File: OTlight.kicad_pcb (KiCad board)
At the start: 2 copper layers, 90 x 55 mm, 70 parts, among them P1 CONN_01X02, P2 CONN_01X14, P3 CONN_01X14, P4 CONN_01X14, P5 CONN_01X14, Q1 TEMT6000, Q2 RSR030N06TL, T1 TRANSFO, U1 LM3478, U12 MAX6931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

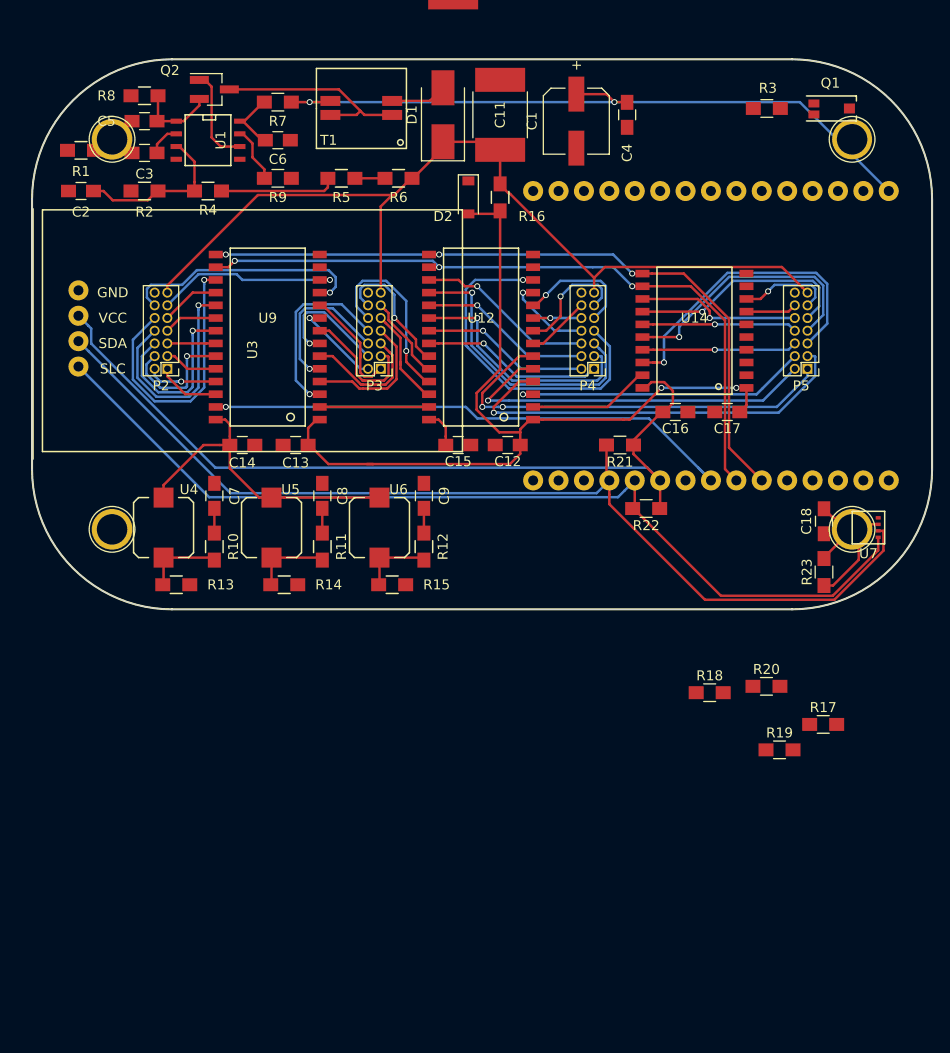
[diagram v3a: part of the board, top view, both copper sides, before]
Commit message: The start of bearing upgrade
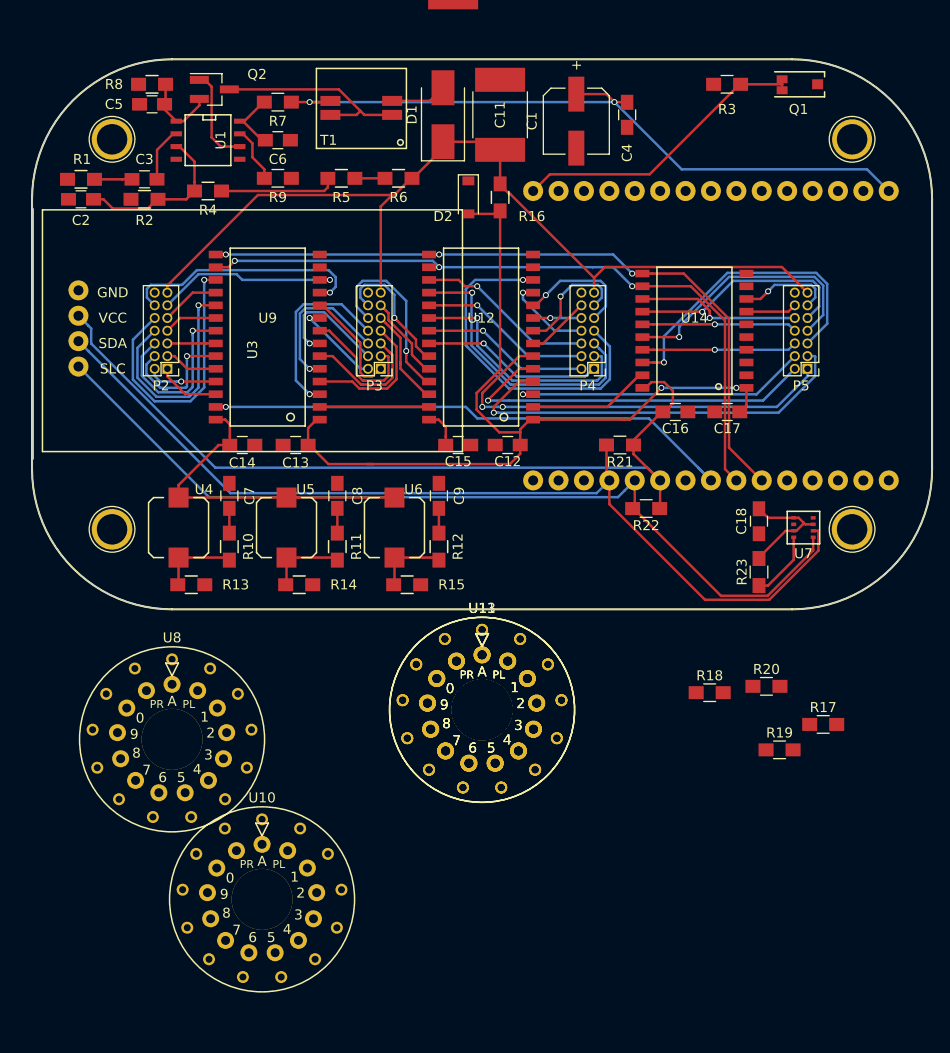
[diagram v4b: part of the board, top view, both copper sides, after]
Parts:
- added U10: IN-14, BamboulabFootprints:IN-14-bearing-7mm, F.Cu at (67.0, 161.0)
- added U11, U13: IN-14, BamboulabFootprints:IN-14-bearing-7mm, F.Cu at (89.0, 142.1)
- added U8: IN-14, BamboulabFootprints:IN-14-bearing-7mm, F.Cu at (58.0, 145.0)
- moved C18 6.50 mm to (116.7, 123.2)
- moved R23 6.50 mm to (116.7, 128.3)
- moved U7 6.50 mm to (121.1, 123.8)
- moved R3 4.65 mm to (113.5, 79.5)
- moved Q1 3.99 mm to (119.0, 79.5)
- moved R1 2.89 mm to (48.9, 89.0)
- moved C3 2.64 mm to (55.2, 89.0)
- moved C5 1.85 mm to (56.0, 81.5)
- moved C7 1.50 mm to (63.7, 120.7)
- moved C8 1.50 mm to (74.5, 120.7)
- moved C9 1.50 mm to (84.7, 120.7)
- moved R10 1.50 mm to (63.7, 125.7)
- moved R11 1.50 mm to (74.5, 125.7)
- moved R12 1.50 mm to (84.7, 125.7)
- moved R13 1.50 mm to (59.9, 129.5)
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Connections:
- R17 pad 1: Net-(R17-Pad1) -> /HVout
- R18 pad 1: Net-(R18-Pad1) -> /HVout
- R19 pad 1: Net-(R19-Pad1) -> /HVout
- R20 pad 1: Net-(R20-Pad1) -> /HVout
- U12 pad 10: Net-(P4-Pad9) -> Net-(U11-Pad10)
- U12 pad 11: Net-(P4-Pad8) -> Net-(U11-Pad9)
- U12 pad 12: Net-(P4-Pad7) -> Net-(U11-Pad8)
- U12 pad 17: Net-(P4-Pad6) -> Net-(U11-Pad7)
- U12 pad 18: Net-(P4-Pad5) -> Net-(U11-Pad6)
- U12 pad 19: Net-(P4-Pad4) -> Net-(U11-Pad5)
- U12 pad 20: Net-(P4-Pad3) -> Net-(U11-Pad4)
- U12 pad 21: Net-(P4-Pad2) -> Net-(U11-Pad3)
- U12 pad 22: Net-(P4-Pad1) -> Net-(U11-Pad12)
- U12 pad 23: Net-(P3-Pad12) -> Net-(U10-Pad13)
- U12 pad 24: Net-(P3-Pad11) -> Net-(U10-Pad2)
- U12 pad 25: Net-(P3-Pad10) -> Net-(U10-Pad11)
- U12 pad 26: Net-(P3-Pad9) -> Net-(U10-Pad10)
- U12 pad 3: Net-(P5-Pad4) -> Net-(U12-Pad3)
- U12 pad 4: Net-(P5-Pad3) -> Net-(U12-Pad4)
- U12 pad 5: Net-(P5-Pad2) -> Net-(U12-Pad5)
- U12 pad 6: Net-(P5-Pad1) -> Net-(U12-Pad6)
- U12 pad 7: Net-(P4-Pad12) -> Net-(U11-Pad13)
- U12 pad 8: Net-(P4-Pad11) -> Net-(U11-Pad2)
- U12 pad 9: Net-(P4-Pad10) -> Net-(U11-Pad11)
- U14 pad 13: Net-(P5-Pad10) -> Net-(U13-Pad11)
- U14 pad 14: Net-(P5-Pad9) -> Net-(U13-Pad10)
- U14 pad 15: Net-(P5-Pad8) -> Net-(U13-Pad9)
- U14 pad 16: Net-(P5-Pad7) -> Net-(U13-Pad8)
- U14 pad 17: Net-(P5-Pad6) -> Net-(U13-Pad7)
- U14 pad 18: Net-(P5-Pad5) -> Net-(U13-Pad6)
- U14 pad 7: Net-(P5-Pad12) -> Net-(U13-Pad13)
- U14 pad 8: Net-(P5-Pad11) -> Net-(U13-Pad2)
- U9 pad 10: Net-(P3-Pad1) -> Net-(U10-Pad12)
- U9 pad 11: Net-(P2-Pad12) -> Net-(U8-Pad13)
- U9 pad 12: Net-(P2-Pad11) -> Net-(U8-Pad2)
- U9 pad 17: Net-(P2-Pad10) -> Net-(U8-Pad11)
- U9 pad 18: Net-(P2-Pad9) -> Net-(U8-Pad10)
- U9 pad 19: Net-(P2-Pad8) -> Net-(U8-Pad9)
- U9 pad 20: Net-(P2-Pad7) -> Net-(U8-Pad8)
- U9 pad 21: Net-(P2-Pad6) -> Net-(U8-Pad7)
- U9 pad 22: Net-(P2-Pad5) -> Net-(U8-Pad6)
- U9 pad 23: Net-(P2-Pad4) -> Net-(U8-Pad5)
- U9 pad 24: Net-(P2-Pad3) -> Net-(U8-Pad4)
- U9 pad 25: Net-(P2-Pad2) -> Net-(U8-Pad3)
- U9 pad 26: Net-(P2-Pad1) -> Net-(U8-Pad12)
- U9 pad 3: Net-(P3-Pad8) -> Net-(U10-Pad9)
- U9 pad 4: Net-(P3-Pad7) -> Net-(U10-Pad8)
- U9 pad 5: Net-(P3-Pad6) -> Net-(U10-Pad7)
- U9 pad 6: Net-(P3-Pad5) -> Net-(U10-Pad6)
- U9 pad 7: Net-(P3-Pad4) -> Net-(U10-Pad5)
- U9 pad 8: Net-(P3-Pad3) -> Net-(U10-Pad4)
- U9 pad 9: Net-(P3-Pad2) -> Net-(U10-Pad3)
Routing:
- net Net-(Q1-Pad2): track 0.00 -> 30.4 mm
- net Net-(R22-Pad2): track 96.0 -> 89.5 mm
- net Net-(R21-Pad2): track 101.8 -> 95.3 mm
- net Net-(U13-Pad10): track 0.00 -> 5.96 mm
- net Net-(P5-Pad9): track 22.8 -> 16.8 mm
- net Net-(U11-Pad8): track 0.00 -> 5.80 mm, vias 0 -> 1
- net Net-(P4-Pad7): track 35.0 -> 29.2 mm, vias 1 -> 0
- net Net-(P3-Pad1): track 11.5 -> 5.91 mm
- net Net-(U10-Pad12): track 0.00 -> 5.61 mm
- net Net-(U13-Pad11): track 0.00 -> 5.54 mm
- net Net-(P5-Pad10): track 16.4 -> 10.9 mm
- net Net-(U11-Pad3): track 0.00 -> 5.39 mm
- net Net-(P4-Pad2): track 16.8 -> 11.4 mm
- net Net-(P4-Pad3): track 24.4 -> 19.6 mm
- net Net-(U11-Pad4): track 0.00 -> 4.82 mm
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
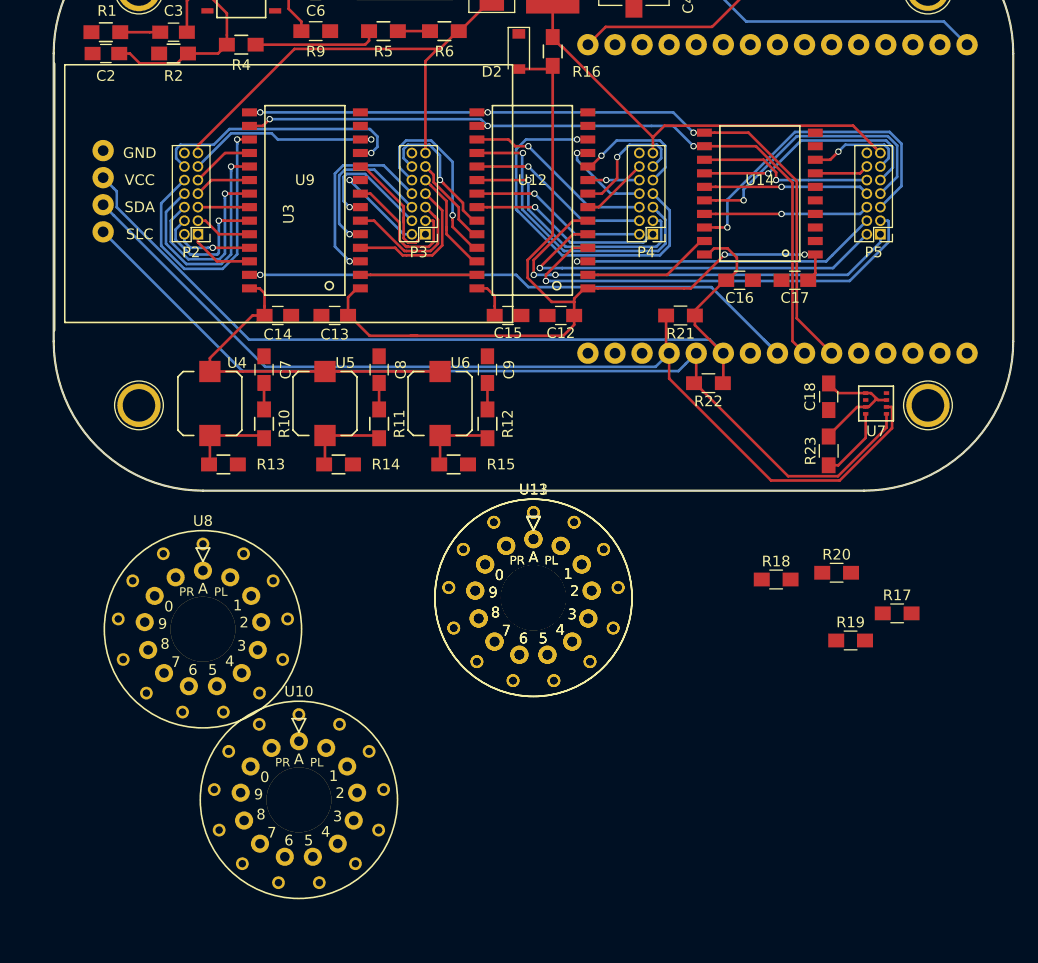
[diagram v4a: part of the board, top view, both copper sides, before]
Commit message: Realigned tubes with bearings, now the tubes are perfectly centered on both x and y axis
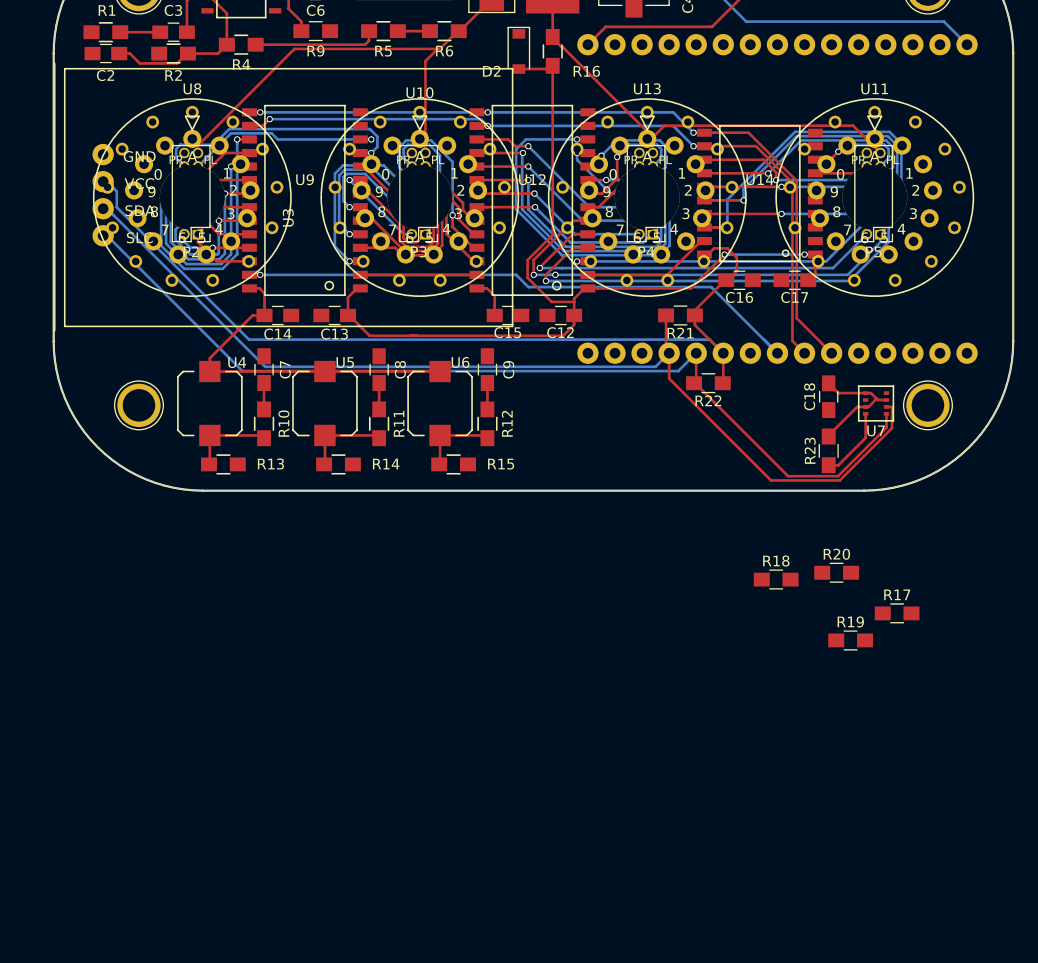
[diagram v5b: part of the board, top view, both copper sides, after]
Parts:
- moved U10 57.6 mm to (78.3, 104.5)
- moved U11 49.3 mm to (121.0, 104.5)
- moved U8 40.5 mm to (57.0, 104.5)
- moved U13 39.0 mm to (99.7, 104.5)
- moved U3 0.37 mm to (66.0, 104.5)
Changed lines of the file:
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@@
-(kicad_pcb (version 4) (host pcbnew 4.0.7)
+(kicad_pcb (version 20171130) (host pcbnew "(2018-01-14 revision 63e55e918)-makepkg")
   (general
-    (links 239)
-    (no_connects 161)
-    (area 43.949999 76.949999 134.050001 132.050001)
     (thickness 1.6)
     (drawings 19)
@@
       (layerselection 0x000f0_80000001)
       (usegerberextensions false)
+      (usegerberattributes false)
+      (usegerberadvancedattributes false)
+      (creategerberjobfile false)
       (excludeedgelayer true)
       (linewidth 0.100000)
@@
       (hpglpenspeed 20)
       (hpglpendiameter 15)
-      (hpglpenoverlay 2)
       (psnegative false)
       (psa4output false)
@@
     (tags "resistor 0805")
     (attr smd)
-    (fp_text reference R12 (at 0 -1.905 450) (layer F.SilkS)
+    (fp_text reference R12 (at 0 -1.905 90) (layer F.SilkS)
       (effects (font (size 1 1) (thickness 0.15)))
     )
@@
     (tags SOD-123)
     (attr smd)
-    (fp_text reference D2 (at 1.905 2.54 540) (layer F.SilkS)
+    (fp_text reference D2 (at 1.905 2.54 180) (layer F.SilkS)
       (effects (font (size 1 1) (thickness 0.15)))
     )
@@
     (tags "capacitor 0805")
     (attr smd)
-    (fp_text reference C4 (at 3.81 0 450) (layer F.SilkS)
+    (fp_text reference C4 (at 3.81 0 90) (layer F.SilkS)
       (effects (font (size 1 1) (thickness 0.15)))
     )
@@
     (tags "resistor 0805")
     (attr smd)
-    (fp_text reference R8 (at 3.81 0 360) (layer F.SilkS)
+    (fp_text reference R8 (at 3.81 0) (layer F.SilkS)
       (effects (font (size 1 1) (thickness 0.15)))
     )
@@
     (tags "resistor 0805")
     (attr smd)
-    (fp_text reference R10 (at 0 -1.905 450) (layer F.SilkS)
+    (fp_text reference R10 (at 0 -1.905 90) (layer F.SilkS)
       (effects (font (size 1 1) (thickness 0.15)))
     )
@@
     (tags "resistor 0805")
     (attr smd)
-    (fp_text reference R16 (at 1.905 -3.175 360) (layer F.SilkS)
+    (fp_text reference R16 (at 1.905 -3.175) (layer F.SilkS)
       (effects (font (size 1 1) (thickness 0.15)))
     )
@@
     (at 26.5176 110.6932)
     (fp_text reference G*** (at 0 0) (layer F.SilkS) hide
-      (effects (font (thickness 0.3)))
+      (effects (font (size 1.524 1.524) (thickness 0.3)))
     )
     (fp_text value LOGO (at 0.75 0) (layer F.SilkS) hide
-      (effects (font (thickness 0.3)))
+      (effects (font (size 1.524 1.524) (thickness 0.3)))
     )
     (fp_poly (pts (xy 0.066496 -3.18191) (xy 0.14042 -3.180865) (xy 0.20835 -3.178867) (xy 0.267395 -3.175902)
@@
       (net 2 GND))
     (model ${KISYS3DMOD}/Pin_Headers.3dshapes/Pin_Header_Straight_1x02_Pitch2.54mm.wrl
-      (at (xyz 0 -0.05 0))
+      (offset (xyz 0 -1.269999980926514 0))
       (scale (xyz 1 1 1))
       (rotate (xyz 0 0 90))
@@
     (at 73.914 192.405)
     (fp_text reference G*** (at 0 0) (layer F.SilkS) hide
-      (effects (font (thickness 0.3)))
+      (effects (font (size 1.524 1.524) (thickness 0.3)))
     )
     (fp_text value LOGO (at 0.75 0) (layer F.SilkS) hide
-      (effects (font (thickness 0.3)))
+      (effects (font (size 1.524 1.524) (thickness 0.3)))
     )
     (fp_poly (pts (xy 7.776308 2.422769) (xy -7.776307 2.422769) (xy -7.776307 1.008304) (xy -7.655194 1.008304)
@@
     (at 144.272 130.048)
     (fp_text reference G*** (at 0 0) (layer F.SilkS) hide
-      (effects (font (thickness 0.3)))
+      (effects (font (size 1.524 1.524) (thickness 0.3)))
     )
     (fp_text value LOGO (at 0.75 0) (layer F.SilkS) hide
-      (effects (font (thickness 0.3)))
+      (effects (font (size 1.524 1.524) (thickness 0.3)))
     )
     (fp_poly (pts (xy -2.603459 -0.236601) (xy -2.492479 -0.183516) (xy -2.407788 -0.092057) (xy -2.355584 0.03253)
@@
     (at 119.253 32.131)
     (fp_text reference G*** (at 0 0) (layer F.SilkS) hide
-      (effects (font (thickness 0.3)))
+      (effects (font (size 1.524 1.524) (thickness 0.3)))
     )
     (fp_text value LOGO (at 0.75 0) (layer F.SilkS) hide
-      (effects (font (thickness 0.3)))
+      (effects (font (size 1.524 1.524) (thickness 0.3)))
     )
     (fp_poly (pts (xy 4.301613 4.301613) (xy -4.301612 4.301613) (xy -4.301612 2.335162) (xy -4.055806 2.335162)
@@
   )
   (module BamboulabFootprints:DS3231 (layer F.Cu)
-    (at 66.04 104.14)
+    (at 66.04 104.51)
     (fp_text reference U3 (at 0 1.905 90) (layer F.SilkS)
       (effects (font (size 1 1) (thickness 0.15)))
@@
   )
   (module BamboulabFootprints:IN-14-bearing-7mm locked (layer F.Cu)
-    (at 58 145)
+    (at 57.004 104.51)
     (fp_text reference U8 (at 0 -10.16) (layer F.SilkS)
       (effects (font (size 1 1) (thickness 0.15)))
@@
   )
   (module BamboulabFootprints:IN-14-bearing-7mm locked (layer F.Cu)
-    (at 67 161)
-    (fp_text reference U10 (at 0 -10.16) (layer F.SilkS)
+    (at 78.34 104.51)
+    (fp_text reference U10 (at 0 -9.79) (layer F.SilkS)
       (effects (font (size 1 1) (thickness 0.15)))
     )
@@
   )
   (module BamboulabFootprints:IN-14-bearing-7mm locked (layer F.Cu)
-    (at 89 142.050001)
+    (at 121.012 104.51)
     (fp_text reference U11 (at 0 -10.16) (layer F.SilkS)
       (effects (font (size 1 1) (thickness 0.15)))
@@
   )
   (module BamboulabFootprints:IN-14-bearing-7mm locked (layer F.Cu)
-    (at 89 142.050001)
+    (at 99.676 104.51)
     (fp_text reference U13 (at 0 -10.16) (layer F.SilkS)
       (effects (font (size 1 1) (thickness 0.15)))

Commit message: Everything in place with bearings sockets.
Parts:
- removed C11: 1u, Capacitors_SMD:C_2220_HandSoldering
- removed G***: LOGO, OTlight:Misakaimouto
- removed G***: LOGO, OTlight:PVUnit
- removed G***: LOGO, OTlight:versionNumb
- removed G***: LOGO, BamboulabFootprints:QRcodeOTL
- removed P2, P3, P4, P5: CONN_01X14, Pin_Headers:Pin_Header_Straight_2x07_Pitch1.27mm
- D1: footprint Diodes_SMD:D_SMB_Handsoldering -> Diodes_SMD:D_SMB-SMC_Universal_Handsoldering
- U10, U11, U13, U8: footprint BamboulabFootprints:IN-14-bearing-7mm -> BamboulabFootprints:bearing-7mm
- U12, U14, U9: moved to B.Cu
- U2: value NodeMCU -> ESP32; footprint BamboulabFootprints:NodeMCU-V2 -> BamboulabFootprints:ESP32-OLED
- moved R17 89.0 mm to (47.5, 96.5)
- moved R22 82.2 mm to (28.5, 150.8), turned to 270 degrees
- moved R21 80.0 mm to (28.5, 145.3), turned to 270 degrees
- moved R18 61.2 mm to (69.0, 96.5)
- moved R19 57.0 mm to (90.5, 96.5)
- moved U3 52.0 mm to (36.0, 147.0)
- moved R20 43.7 mm to (111.0, 96.5)
- moved C12 43.5 mm to (68.8, 78.5), turned to 180 degrees
- moved C13 40.9 mm to (87.8, 78.5), turned to 180 degrees
- moved C14 34.6 mm to (47.5, 85.8), turned to 270 degrees
- moved C15 29.2 mm to (68.8, 92.5)
- moved C16 27.0 mm to (109.5, 85.2), turned to 90 degrees
- moved C17 27.0 mm to (113.0, 85.2), turned to 270 degrees
- moved U11 21.3 mm to (99.7, 104.5)
- moved U13 21.3 mm to (121.0, 104.5)
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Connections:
- U2 pad 1: Net-(Q1-Pad2) -> Net-(U2-Pad1)
- U2 pad 10: GND -> Net-(U2-Pad10)
- U2 pad 14: GND -> Net-(U2-Pad14)
- U2 pad 15: +5V -> Net-(U2-Pad15)
- U2 pad 16: +3V3 -> Net-(U2-Pad16)
- U2 pad 17: GND -> Net-(U2-Pad17)
- U2 pad 20: Net-(C9-Pad1) -> Net-(U2-Pad20)
- U2 pad 21: /CLK -> Net-(U2-Pad21)
- U2 pad 22: /LOAD -> Net-(U2-Pad22)
- U2 pad 23: /DIN -> Net-(U2-Pad23)
- U2 pad 24: GND -> Net-(U2-Pad24)
- U2 pad 25: +3V3 -> Net-(U2-Pad25)
- U2 pad 26: Net-(R22-Pad2) -> Net-(U2-Pad26)
- U2 pad 27: Net-(R21-Pad2) -> Net-(U2-Pad27)
- U2 pad 28: Net-(C8-Pad1) -> Net-(U2-Pad28)
- U2 pad 29: Net-(C7-Pad1) -> Net-(U2-Pad29)
- U2 pad 8: GND -> Net-(U2-Pad8)
- U2 pad 9: +3V3 -> Net-(U2-Pad9)
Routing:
- net +3V3: track 134.2 -> 0.00 mm
- net Net-(R21-Pad2): track 95.3 -> 0.00 mm
- net Net-(R22-Pad2): track 89.5 -> 0.00 mm
- net Net-(C12-Pad2): track 85.3 -> 2.15 mm, vias 2 -> 0
- net /CLK: track 72.5 -> 0.00 mm, vias 3 -> 0
- net /LOAD: track 71.5 -> 0.00 mm, vias 3 -> 0
- net Net-(U11-Pad11): track 1.73 -> 71.4 mm
- net Net-(U11-Pad10): track 1.70 -> 64.7 mm, vias 1 -> 0
- net Net-(U12-Pad3): track 1.44 -> 61.9 mm, vias 1 -> 0
- net Net-(U13-Pad9): track 1.07 -> 58.8 mm
- net Net-(U13-Pad11): track 5.54 -> 62.7 mm
- net Net-(U10-Pad3): track 1.01 -> 58.1 mm
- net Net-(U13-Pad6): track 1.26 -> 58.3 mm
- net Net-(U11-Pad9): track 1.01 -> 57.2 mm
- net Net-(U12-Pad4): track 1.39 -> 56.3 mm
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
